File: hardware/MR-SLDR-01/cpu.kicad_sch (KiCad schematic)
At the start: 25 parts, among them J4 Conn_02x05_Odd_Even, U5 CP2102N-Axx-xQFN28

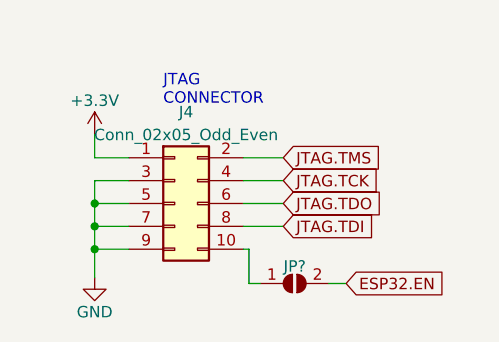
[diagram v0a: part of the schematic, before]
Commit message: v0.8 MM added rangefinder; move bt handler from main.c to slider_bt.c
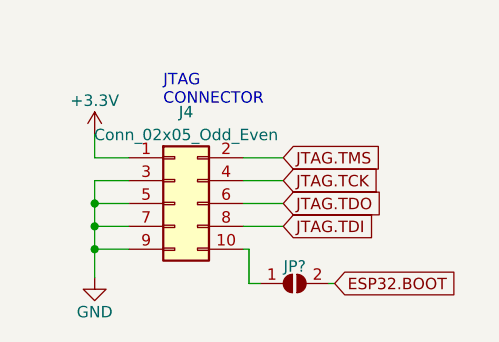
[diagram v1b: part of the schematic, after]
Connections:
- net ESP32.BOOT: now also JP?.2 (B)
- net ESP32.EN: no longer JP?.2 (B)
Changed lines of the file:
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@@
     (stroke (width 0) (type default))
   )
-  (wire (pts (xy 269.875 149.86) (xy 271.78 149.86))
+  (wire (pts (xy 269.875 149.86) (xy 270.51 149.86))
     (stroke (width 0) (type default))
   )
@@
     )
   )
-  (global_label "ESP32.EN" (shape input) (at 271.78 149.86 0) (fields_autoplaced)
-    (effects (font (size 1.27 1.27)) (justify left))
-    (property "Intersheetrefs" "${INTERSHEET_REFS}" (at 283.8176 149.86 0)
-      (effects (font (size 1.27 1.27)) (justify left) hide)
-    )
+  (global_label "ESP32.BOOT" (shape input) (at 270.51 149.86 0) (fields_autoplaced)
+    (effects (font (size 1.27 1.27)) (justify left))
+    (property "Intersheetrefs" "${INTERSHEET_REFS}" (at 284.9667 149.86 0)
+      (effects (font (size 1.27 1.27)) (justify left) hide)
+    )
